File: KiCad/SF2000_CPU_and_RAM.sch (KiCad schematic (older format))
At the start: 5 parts, among them U10 68000D, U14 IS61WV20488FBLL-10TLI, U15 IS61WV20488FBLL-10TLI, U16 IS61WV20488FBLL-10TLI, U17 IS61WV20488FBLL-10TLI

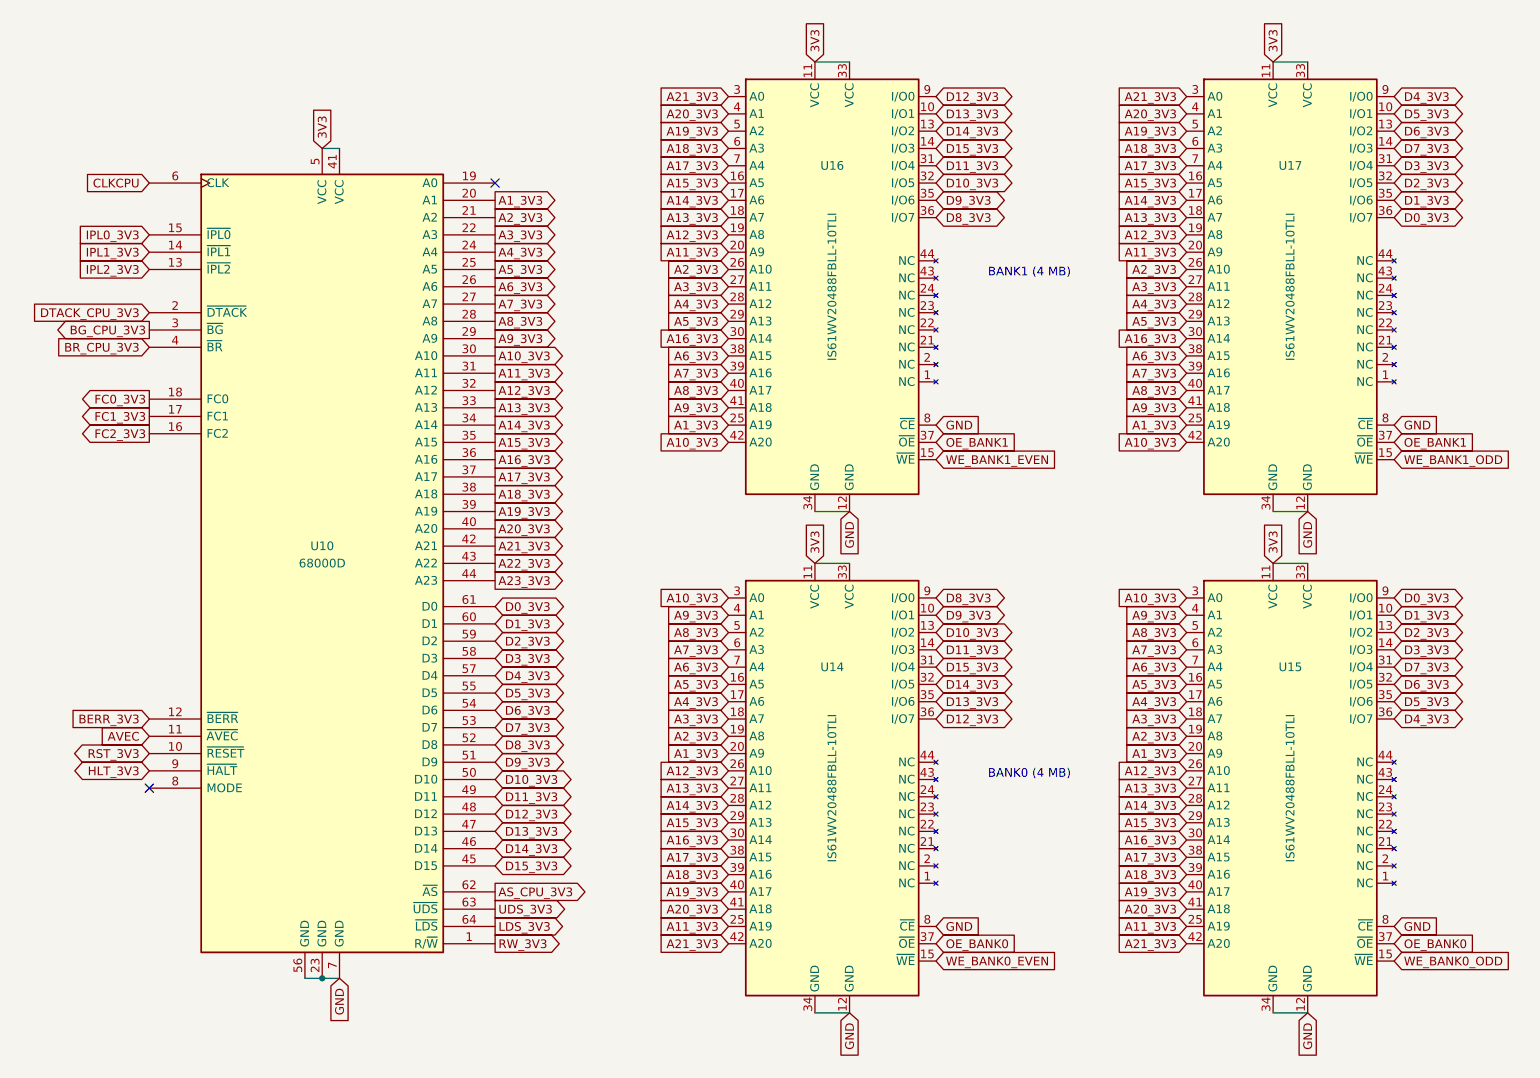
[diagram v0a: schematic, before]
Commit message: Start major redesign, remove U11 (SST39LF802C), remove U13 (SST39LF040), replaced U8 (T8Q144C3) with 10M02SCU324C8G, replaced U7 (74LVC2G86) with 74LVC1G57GV, adding SDRAM in BGA54 (IM1216SDBABG-6I)
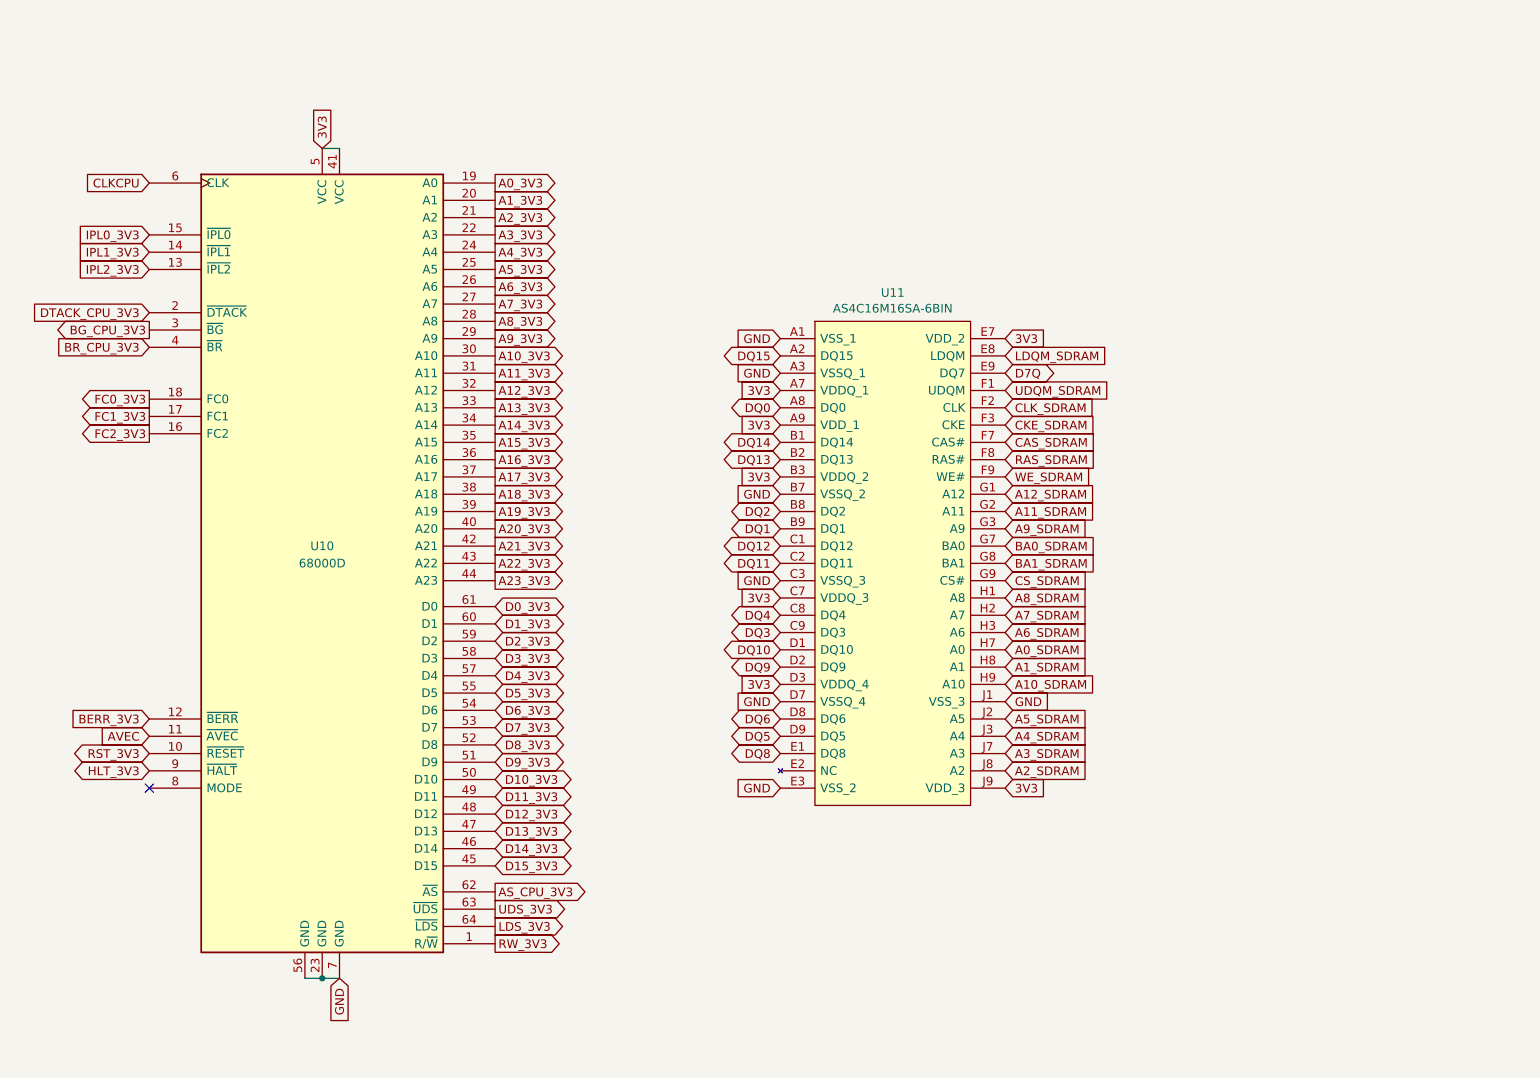
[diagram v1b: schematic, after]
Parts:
- removed U14, U15, U16, U17: IS61WV20488FBLL-10TLI, Package_SO:TSOP-II-44_10.16x18.41mm_P0.8mm, symbol SF2000:IS61WV20488FBLL-10TLI
- added U11: AS4C16M16SA-6BIN, SF2000:BGA54C80P9X9_800X800X120, symbol SF2000:AS4C16M16SA-6BIN
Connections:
- net 3V3: now also U11.A7 (VDDQ_1), U11.A9 (VDD_1), U11.B3 (VDDQ_2), U11.C7 (VDDQ_3), U11.D3 (VDDQ_4), U11.E7 (VDD_2), U11.J9 (VDD_3)
- net GND: now also U11.A1 (VSS_1), U11.A3 (VSSQ_1), U11.B7 (VSSQ_2), U11.C3 (VSSQ_3), U11.D7 (VSSQ_4), U11.E3 (VSS_2), U11.J1 (VSS_3)
- net A0_3V3: now reaches U10.19 (A0)
- new net A0_SDRAM: U11.H7 (A0)
- new net A10_SDRAM: U11.H9 (A10)
- new net A11_SDRAM: U11.G2 (A11)
- new net A12_SDRAM: U11.G1 (A12)
- new net A1_SDRAM: U11.H8 (A1)
- new net A2_SDRAM: U11.J8 (A2)
- new net A3_SDRAM: U11.J7 (A3)
- new net A4_SDRAM: U11.J3 (A4)
- new net A5_SDRAM: U11.J2 (A5)
- new net A6_SDRAM: U11.H3 (A6)
- new net A7_SDRAM: U11.H2 (A7)
- new net A8_SDRAM: U11.H1 (A8)
- new net A9_SDRAM: U11.G3 (A9)
- new net BA0_SDRAM: U11.G7 (BA0)
- new net BA1_SDRAM: U11.G8 (BA1)
- new net CAS_SDRAM: U11.F7 (CAS#)
- new net CKE_SDRAM: U11.F3 (CKE)
- new net CLK_SDRAM: U11.F2 (CLK)
- new net CS_SDRAM: U11.G9 (CS#)
- new net D7Q: U11.E9 (DQ7)
- new net DQ0: U11.A8 (DQ0)
- new net DQ1: U11.B9 (DQ1)
- new net DQ10: U11.D1 (DQ10)
- new net DQ11: U11.C2 (DQ11)
- new net DQ12: U11.C1 (DQ12)
- new net DQ13: U11.B2 (DQ13)
- new net DQ14: U11.B1 (DQ14)
- new net DQ15: U11.A2 (DQ15)
- new net DQ2: U11.B8 (DQ2)
- new net DQ3: U11.C9 (DQ3)
- new net DQ4: U11.C8 (DQ4)
- new net DQ5: U11.D9 (DQ5)
- new net DQ6: U11.D8 (DQ6)
- new net DQ8: U11.E1 (DQ8)
- new net DQ9: U11.D2 (DQ9)
- new net LDQM_SDRAM: U11.E8 (LDQM)
- new net RAS_SDRAM: U11.F8 (RAS#)
- new net UDQM_SDRAM: U11.F1 (UDQM)
- new net WE_SDRAM: U11.F9 (WE#)
- no-connect marks 2 -> 1
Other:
- note removed: "BANK0 (4 MB)"
- note removed: "BANK1 (4 MB)"
